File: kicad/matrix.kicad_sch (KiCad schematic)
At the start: 72 parts, among them SW401 SW_Push_Dual, SW402 SW_Push_Dual, SW403 SW_Push_Dual, SW404 SW_Push_Dual, SW405 SW_Push_Dual, SW406 SW_Push_Dual, SW407 SW_Push_Dual, SW408 SW_Push_Dual, SW409 SW_Push_Dual, SW410 SW_Push_Dual, SW411 SW_Push_Dual, SW412 SW_Push_Dual, SW413 SW_Push_Dual, SW414 SW_Push_Dual, SW415 SW_Push_Dual, SW416 SW_Push_Dual, SW417 SW_Push_Dual, SW418 SW_Push_Dual, SW419 SW_Push_Dual, SW420 SW_Push_Dual, SW421 SW_Push_Dual, SW422 SW_Push_Dual, SW423 SW_Push_Dual, SW424 SW_Push_Dual, SW425 SW_Push_Dual, SW426 SW_Push_Dual, SW427 SW_Push_Dual, SW428 SW_Push_Dual, SW429 SW_Push_Dual, SW430 SW_Push_Dual, SW431 SW_Push_Dual, SW432 SW_Push_Dual, SW433 SW_Push_Dual, SW434 SW_Push_Dual, SW435 SW_Push_Dual, SW436 SW_Push_Dual

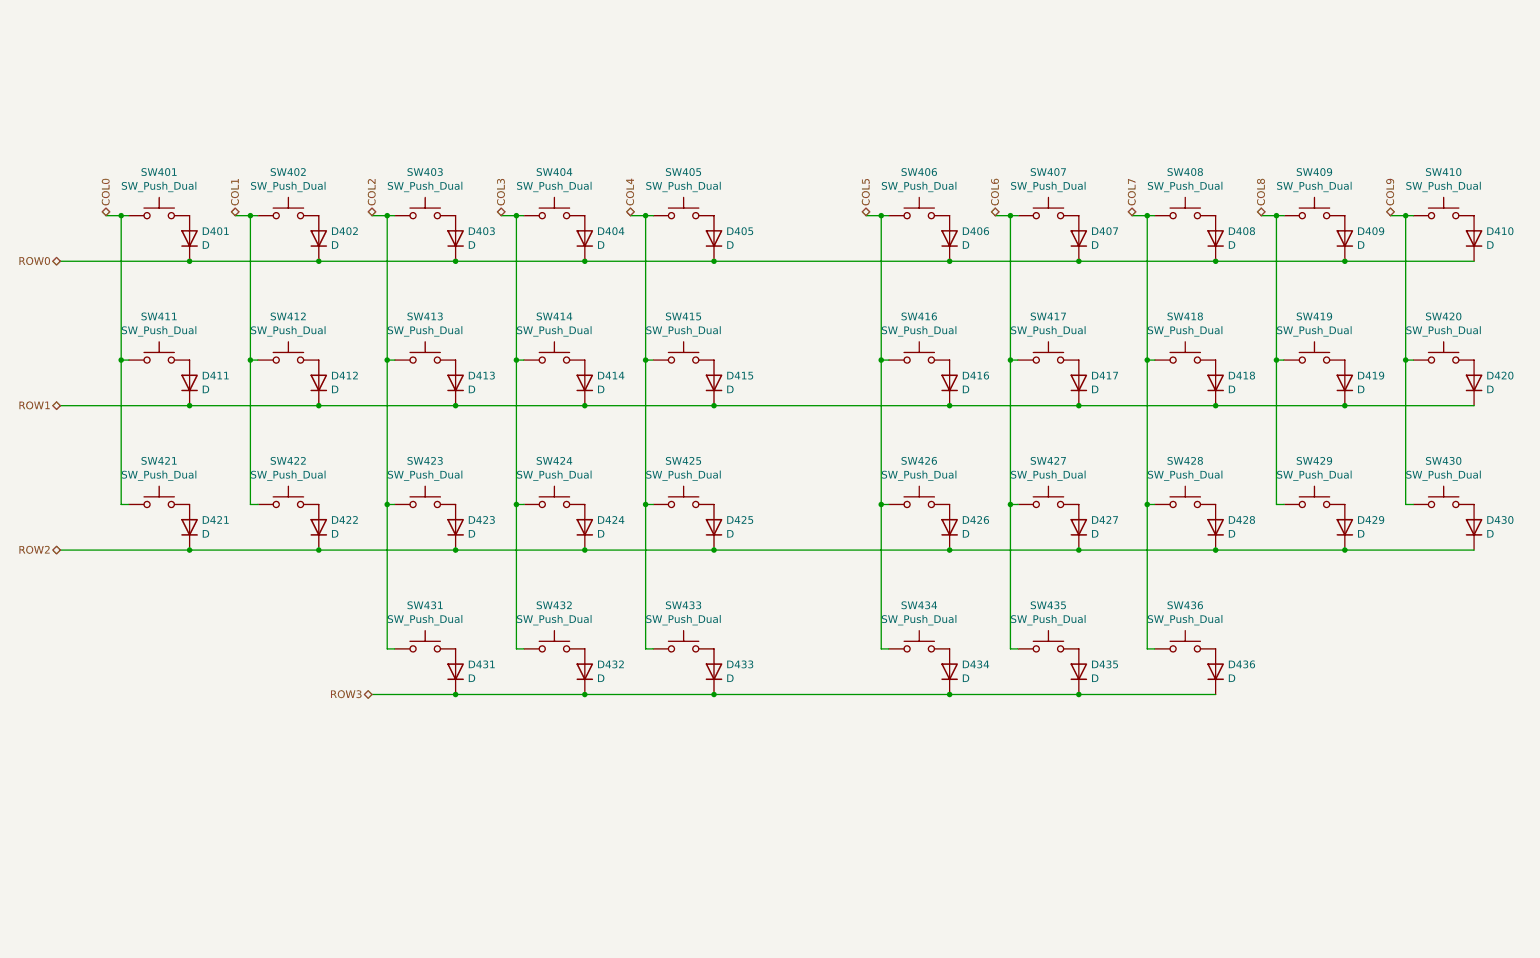
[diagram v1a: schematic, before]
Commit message: changed from rp2040 to nrf
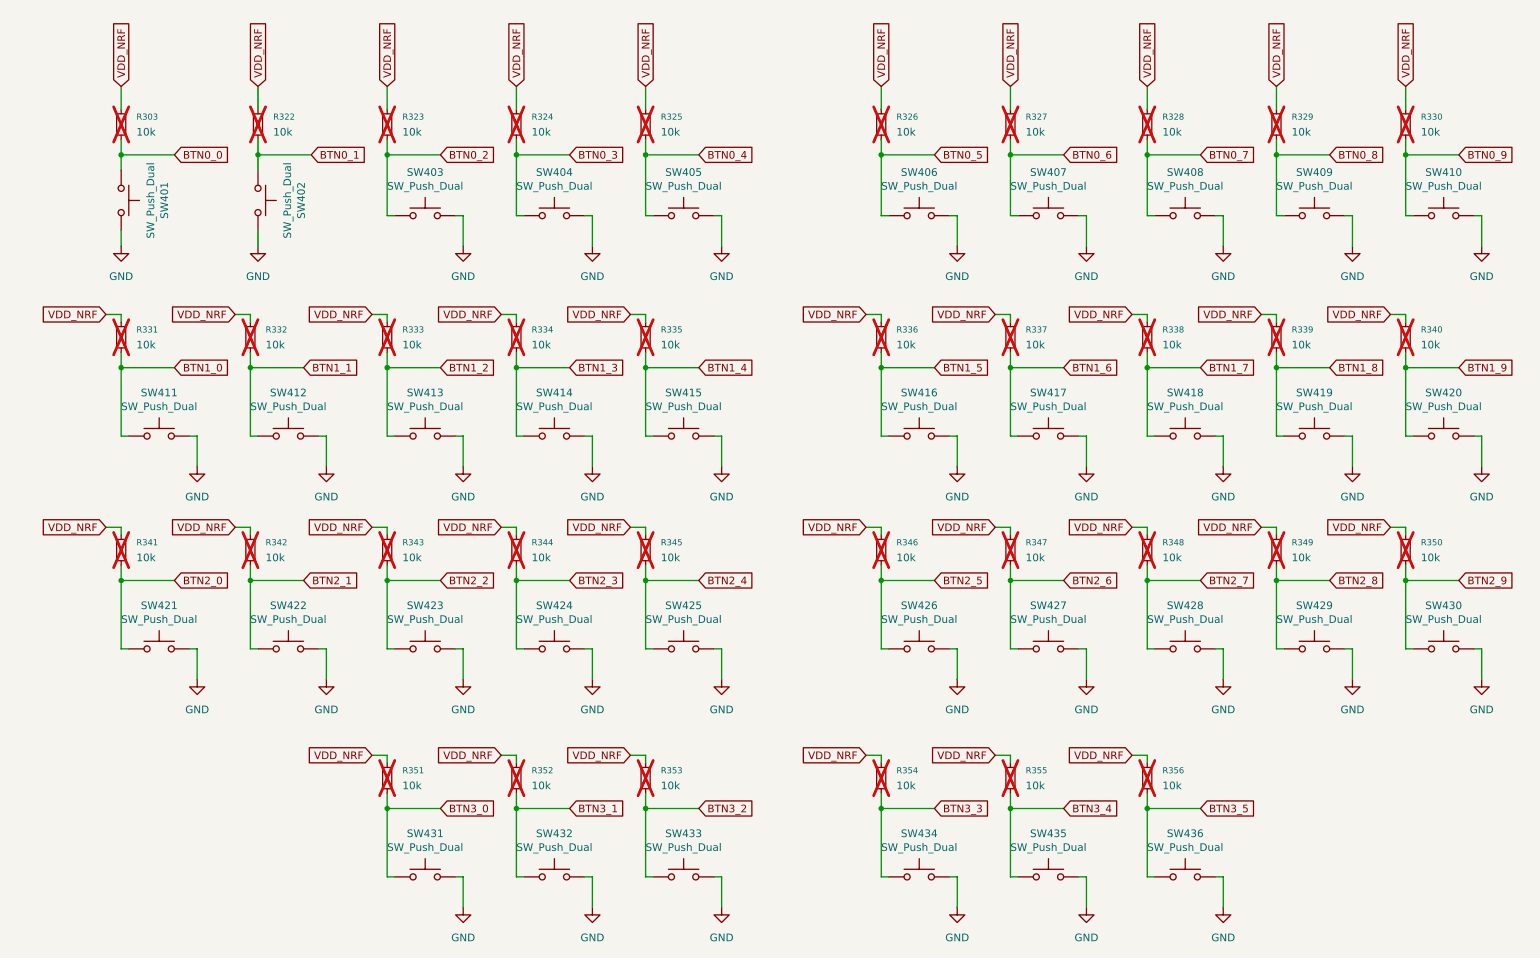
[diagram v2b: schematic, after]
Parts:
- removed D401, D402, D403, D404, D405, D406, D407, D408, D409, D410, D411, D412, D413, D414, D415, D416, D417, D418, D419, D420, D421, D422, D423, D424, D425, D426, D427, D428, D429, D430, D431, D432, D433, D434, D435, D436: D, Diode_SMD:D_SOD-123, symbol Device:D
- added R303, R322, R323, R324, R325, R326, R327, R328, R329, R330, R331, R332, R333, R334, R335, R336, R337, R338, R339, R340, R341, R342, R343, R344, R345, R346, R347, R348, R349, R350, R351, R352, R353, R354, R355, R356: 10k, Resistor_SMD:R_0603_1608Metric, symbol Device:R_Small
- SW401, SW402, SW403, SW404, SW405, SW406, SW407, SW408, SW409, SW410, SW411, SW412, SW413, SW414, SW415, SW416, SW417, SW418, SW419, SW420, SW421, SW422, SW423, SW424, SW425, SW426, SW427, SW428, SW429, SW430, SW431, SW432, SW433, SW434, SW435, SW436: footprint Button_Switch_THT:SW_PUSH_6mm -> Button_Switch_THT:SW_PUSH_6mm_H7.3mm
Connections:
- net GND: now reaches SW404.2
- net GND: now also SW401.2, SW402.2, SW403.2, SW405.2, SW406.2, SW407.2, SW408.2, SW409.2, SW410.2, SW411.2, SW412.2, SW413.2, SW414.2, SW415.2, SW416.2, SW417.2, SW418.2, SW419.2, SW420.2, SW421.2, SW422.2, SW423.2, SW424.2, SW425.2, SW426.2, SW427.2, SW428.2, SW429.2, SW430.2, SW431.2, SW432.2, SW433.2, SW434.2, SW435.2, SW436.2
- removed net COL0: SW401.1, SW411.1, SW421.1
- removed net COL1: SW402.1, SW412.1, SW422.1
- removed net COL2: SW403.1, SW413.1, SW423.1, SW431.1
- removed net COL3: SW404.1, SW414.1, SW424.1, SW432.1
- removed net COL4: SW405.1, SW415.1, SW425.1, SW433.1
- removed net COL5: SW406.1, SW416.1, SW426.1, SW434.1
- removed net COL6: SW407.1, SW417.1, SW427.1, SW435.1
- removed net COL7: SW408.1, SW418.1, SW428.1, SW436.1
- removed net COL8: SW409.1, SW419.1, SW429.1
- removed net COL9: SW410.1, SW420.1, SW430.1
- new net BTN0_0: R303.2, SW401.1
- new net BTN0_1: R322.2, SW402.1
- new net BTN0_2: R323.2, SW403.1
- new net BTN0_3: R324.2, SW404.1
- new net BTN0_4: R325.2, SW405.1
- new net BTN0_5: R326.2, SW406.1
- new net BTN0_6: R327.2, SW407.1
- new net BTN0_7: R328.2, SW408.1
- new net BTN0_8: R329.2, SW409.1
- new net BTN0_9: R330.2, SW410.1
- new net BTN1_0: R331.2, SW411.1
- new net BTN1_1: R332.2, SW412.1
- new net BTN1_2: R333.2, SW413.1
- new net BTN1_3: R334.2, SW414.1
- new net BTN1_4: R335.2, SW415.1
- new net BTN1_5: R336.2, SW416.1
- new net BTN1_6: R337.2, SW417.1
- new net BTN1_7: R338.2, SW418.1
- new net BTN1_8: R339.2, SW419.1
- new net BTN1_9: R340.2, SW420.1
- new net BTN2_0: R341.2, SW421.1
- new net BTN2_1: R342.2, SW422.1
- new net BTN2_2: R343.2, SW423.1
- new net BTN2_3: R344.2, SW424.1
- new net BTN2_4: R345.2, SW425.1
- new net BTN2_5: R346.2, SW426.1
- new net BTN2_6: R347.2, SW427.1
- new net BTN2_7: R348.2, SW428.1
- new net BTN2_8: R349.2, SW429.1
- new net BTN2_9: R350.2, SW430.1
- new net BTN3_0: R351.2, SW431.1
- new net BTN3_1: R352.2, SW432.1
- new net BTN3_2: R353.2, SW433.1
- new net BTN3_3: R354.2, SW434.1
- new net BTN3_4: R355.2, SW435.1
- new net BTN3_5: R356.2, SW436.1
- new net VDD_NRF: R303.1, R322.1, R323.1, R324.1, R325.1, R326.1, R327.1, R328.1, R329.1, R330.1, R331.1, R332.1, R333.1, R334.1, R335.1, R336.1, R337.1, R338.1, R339.1, R340.1, R341.1, R342.1, R343.1, R344.1, R345.1, R346.1, R347.1, R348.1, R349.1, R350.1, R351.1, R352.1, R353.1, R354.1, R355.1, R356.1
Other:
- moved on the sheet: SW401, SW402, SW411, SW412, SW413, SW414, SW415, SW416, SW417, SW418, SW419, SW420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

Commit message: board routed
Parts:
- removed R303, R322, R323, R324, R325, R326, R327, R328, R329, R330, R331, R332, R333, R334, R335, R336, R337, R338, R339, R340, R341, R342, R343, R344, R345, R346, R347, R348, R349, R350, R351, R352, R353, R354, R355, R356: 10k, Resistor_SMD:R_0603_1608Metric, symbol Device:R_Small
- added D401, D402, D403, D404, D405, D406, D407, D408, D409, D411, D412, D413, D414, D415, D416, D417, D418, D419, D420, D421, D422, D423, D424, D425, D426, D427, D428, D429, D430, D431, D432, D433, D434, D435, D436: D, Diode_SMD:D_SOD-123, symbol Device:D
- SW401, SW402, SW403, SW404, SW405, SW406, SW407, SW408, SW409, SW410, SW411, SW412, SW413, SW414, SW415, SW416, SW417, SW418, SW419, SW420, SW421, SW422, SW423, SW424, SW425, SW426, SW427, SW428, SW429, SW430, SW431, SW432, SW433, SW434, SW435, SW436: footprint Button_Switch_THT:SW_PUSH_6mm_H7.3mm -> Button_Switch_THT:SW_PUSH_6mm
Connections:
- net BTN1_0 is gone; now on net COL0: SW411.1
- net BTN1_1 is gone; now on net COL1: SW412.1
- net BTN1_2 is gone; now on net COL2: SW413.1
- net BTN1_3 is gone; now on net COL3: SW414.1
- net BTN1_4 is gone; now on net COL4: SW415.1
- net BTN1_5 is gone; now on net COL5: SW416.1
- net BTN1_6 is gone; now on net COL6: SW417.1
- net BTN1_7 is gone; now on net COL7: SW418.1
- net BTN1_8 is gone; now on net COL8: SW419.1
- net BTN2_0 is gone; now on net COL0: SW421.1
- net BTN2_1 is gone; now on net COL1: SW422.1
- net BTN2_2 is gone; now on net COL2: SW423.1
- net BTN2_3 is gone; now on net COL3: SW424.1
- net BTN2_4 is gone; now on net COL4: SW425.1
- net BTN2_5 is gone; now on net COL5: SW426.1
- net BTN2_6 is gone; now on net COL6: SW427.1
- net BTN2_7 is gone; now on net COL7: SW428.1
- net BTN2_8 is gone; now on net COL8: SW429.1
- net BTN2_9 is gone; now on net COL9: SW430.1
- net BTN3_0 is gone; now on net COL2: SW431.1
- net BTN3_1 is gone; now on net COL3: SW432.1
- net BTN3_2 is gone; now on net COL4: SW433.1
- net BTN3_3 is gone; now on net COL5: SW434.1
- net BTN3_4 is gone; now on net COL6: SW435.1
- net BTN3_5 is gone; now on net COL7: SW436.1
- net GND: no longer SW401.2, SW402.2, SW403.2, SW404.2, SW405.2, SW406.2, SW407.2, SW408.2, SW409.2, SW411.2, SW412.2, SW413.2, SW414.2, SW415.2, SW416.2, SW417.2, SW418.2, SW419.2, SW420.2, SW421.2, SW422.2, SW423.2, SW424.2, SW425.2, SW426.2, SW427.2, SW428.2, SW429.2, SW430.2, SW431.2, SW432.2, SW433.2, SW434.2, SW435.2, SW436.2
- net BTN0_0 renamed COL0
- net BTN0_1 renamed COL1
- net BTN0_2 renamed COL2
- net BTN0_3 renamed COL3
- net BTN0_4 renamed COL4
- net BTN0_5 renamed COL5
- net BTN0_6 renamed COL6
- net BTN0_7 renamed COL7
- net BTN0_8 renamed COL8
- net BTN0_9 renamed P_BTN
- net BTN1_9 renamed COL9
- new net: D404.2 (A), SW404.2
- new net: D401.2 (A), SW401.2
- new net: D425.2 (A), SW425.2
- new net: D408.2 (A), SW408.2
- new net: D405.2 (A), SW405.2
- new net: D422.2 (A), SW422.2
- new net: D426.2 (A), SW426.2
- new net: D414.2 (A), SW414.2
- new net: D434.2 (A), SW434.2
- new net: D436.2 (A), SW436.2
- new net: D412.2 (A), SW412.2
- new net: D428.2 (A), SW428.2
- new net: D403.2 (A), SW403.2
- new net: D424.2 (A), SW424.2
- new net: D416.2 (A), SW416.2
- new net: D435.2 (A), SW435.2
- new net: D402.2 (A), SW402.2
- new net: D420.2 (A), SW420.2
- new net: D430.2 (A), SW430.2
- new net: D415.2 (A), SW415.2
- new net: D419.2 (A), SW419.2
- new net: D433.2 (A), SW433.2
- new net: D417.2 (A), SW417.2
- new net: D432.2 (A), SW432.2
- new net: D411.2 (A), SW411.2
- new net: D429.2 (A), SW429.2
- new net: D407.2 (A), SW407.2
- new net: D418.2 (A), SW418.2
- new net: D431.2 (A), SW431.2
- new net: D409.2 (A), SW409.2
- new net: D413.2 (A), SW413.2
- new net: D427.2 (A), SW427.2
- new net: D423.2 (A), SW423.2
- new net: D406.2 (A), SW406.2
- new net: D421.2 (A), SW421.2
- new net ROW0: D401.1 (K), D402.1 (K), D403.1 (K), D404.1 (K), D405.1 (K), D406.1 (K), D407.1 (K), D408.1 (K), D409.1 (K)
- new net ROW1: D411.1 (K), D412.1 (K), D413.1 (K), D414.1 (K), D415.1 (K), D416.1 (K), D417.1 (K), D418.1 (K), D419.1 (K), D420.1 (K)
- new net ROW2: D421.1 (K), D422.1 (K), D423.1 (K), D424.1 (K), D425.1 (K), D426.1 (K), D427.1 (K), D428.1 (K), D429.1 (K), D430.1 (K)
- new net ROW3: D431.1 (K), D432.1 (K), D433.1 (K), D434.1 (K), D435.1 (K), D436.1 (K)
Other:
- moved on the sheet: SW401, SW402, SW403, SW404, SW405, SW406, SW407, SW408, SW409, SW410, SW411, SW412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
